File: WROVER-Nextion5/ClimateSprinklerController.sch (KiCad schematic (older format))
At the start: 177 parts, among them J1 7.5 TO 40 V, J10 HVAC, J2 USB_B_Micro, J3 POWER_SEL, J4 NEXTION, J5 SERIAL, J6 SPI, J7 PIR, J8 I2C, J9 IO_EXP, K1 G6E-134P-US DC5, Q1 MMSS8050, Q2 MMSS8050, Q3 TEPT5700, Q4 2N7002, Q5 2N6073B, Q6 2N6073B, Q7 2N6073B, Q8 2N6073B, Q9 2N6073B, SW1 POWER, SW2 RESET, SW3 MODE, U1 ESP32-WROVER, U10 SHTC3, U11 TMP117, U12 MOC3043, U13 MOC3043, U14 MOC3043, U15 MOC3043, U16 MOC3043, U17 DHT22, U2 MCP23017_SO, U3 FT232RL, U4 TPS22917DBV, U5 LMR36520, U6 SGP40-Sensor_Air_Quality, U7 BME680, U8 LD1086DT33TR, U9 BME280

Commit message: Nextion PCBs tweak
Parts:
- R12, R20: Part RC0805FR-07100KL -> RC0805FR-074R7L
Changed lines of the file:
@@
 F 2 "Resistor_SMD:R_0805_2012Metric_Pad1.20x1.40mm_HandSolder" V 9180 12150 50  0001 C CNN
 F 3 "~" H 9250 12150 50  0001 C CNN
-F 4 "RC0805FR-07100KL" H 9250 12150 50  0001 C CNN "Part"
+F 4 "RC0805FR-074R7L" H 9250 12150 50  0001 C CNN "Part"
 	1    9250 12150
 	1    0    0    -1
@@
 F 2 "Resistor_SMD:R_0805_2012Metric_Pad1.20x1.40mm_HandSolder" V 5980 4700 50  0001 C CNN
 F 3 "~" H 6050 4700 50  0001 C CNN
-F 4 "RC0805FR-07100KL" H 6050 4700 50  0001 C CNN "Part"
+F 4 "RC0805FR-074R7L" H 6050 4700 50  0001 C CNN "Part"
 	1    6050 4700
 	-1   0    0    1

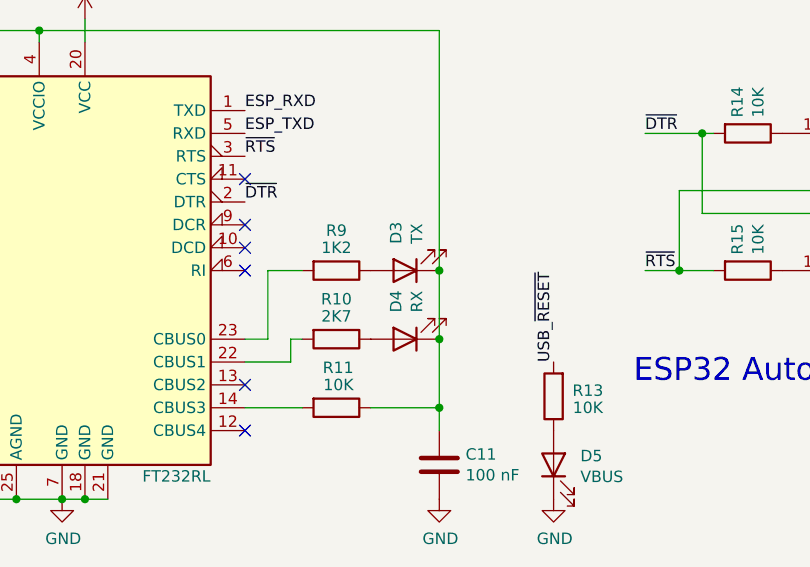
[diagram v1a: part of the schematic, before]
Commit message: TX+RX LEDs were backwards...oops
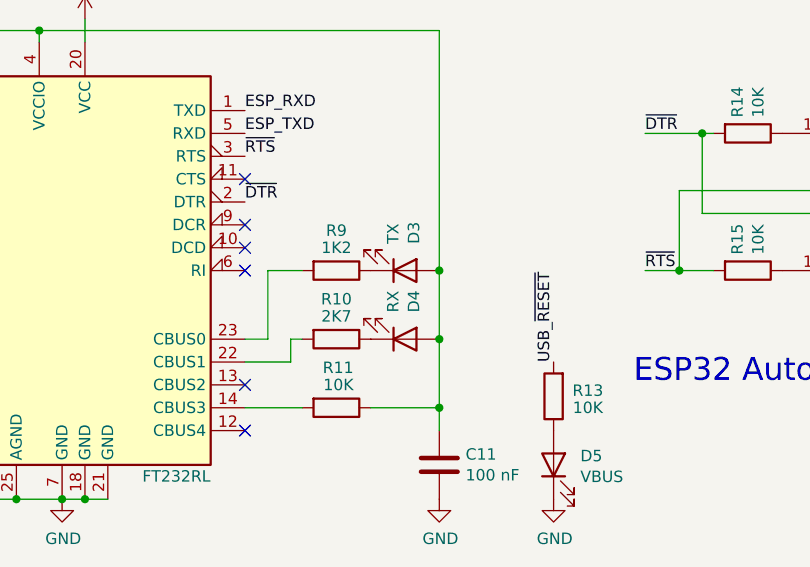
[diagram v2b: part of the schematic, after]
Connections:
- net at C11.1, R11.1, U3.17 (3V3OUT)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: now also D3.2 (A), D4.2 (A); no longer D3.1 (K), D4.1 (K)
- net at R9.1: now also D3.1 (K); no longer D3.2 (A)
- net at R10.1: now also D4.1 (K); no longer D4.2 (A)
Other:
- moved on the sheet: D3, D4
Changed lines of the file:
@@
 F 4 "APTL3216QBC/D" V 5850 12900 50  0001 C CNN "Part"
 	1    5850 12900
-	-1   0    0    1
+	1    0    0    1
 $EndComp
 $Comp
@@
 F 4 "APTL3216SURCK" V 5850 13200 50  0001 C CNN "Part"
 	1    5850 13200
-	-1   0    0    1
+	1    0    0    1
 $EndComp
 Wire Wire Line

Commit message: Doc updates, new images, new enclosures, regenerate gerbers
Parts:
- C1: MPN1 (none) -> C2012X5R1V106K085AC; Part C2012X5R1V106K085AC -> (none)
- C10, C11, C15, C17, C22, C23, C24, C26, C28, C29, C3, C30, C31, C32, C4, C6, C8: MPN1 (none) -> CC0805KRX7R7BB104; Part CC0805KRX7R7BB104 -> (none)
- C12, C2, C5, C9: MPN1 (none) -> C2012X5R1H475K125AB; Part C2012X5R1H475K125AB -> (none)
- C13: MPN1 (none) -> C2012X5R1H224K125AA; Part C2012X5R1H224K125AA -> (none)
- C14, C19, C20: MPN1 (none) -> C0805C105K4RACTU; Part C0805C105K4RACTU -> (none)
- C16, C18, C21: MPN1 (none) -> GRM32ER61C476KE15L; Part GRM32ER61C476KE15L -> (none)
- C25, C27: MPN1 (none) -> EEE-HP0J100R; Part EEE-HP0J100R -> (none)
- C33, C34, C35, C36, C37: MPN1 (none) -> CC0805KRX7R9BB103; Part CC0805KRX7R9BB103 -> (none)
- C7: MPN1 (none) -> UVK1H471MPD; Part UVK1H471MPD -> (none)
- D1: value MBR230S1F-7 -> N/A; MPN1 (none) -> MBR230S1F-7; Part MBR230S1F-7 -> (none)
- D10: MPN1 (none) -> APTL3216CGCK; Part APTL3216CGCK -> (none)
- D11, D5: MPN1 (none) -> APTL3216ZGC; Part APTL3216ZGC -> (none)
- D12, D13, D3: MPN1 (none) -> APTL3216QBC/D; Part APTL3216QBC/D -> (none)
- D14, D15, D4: MPN1 (none) -> APTL3216SURCK; Part APTL3216SURCK -> (none)
- D2: value CD-MBL206SL -> N/A; MPN1 (none) -> CD-MBL206SL; Part CD-MBL206SL -> (none)
- D6, D7: MPN1 (none) -> 597-6901-607F; Part 597-6901-607F -> (none)
- D8: MPN1 (none) -> APTL3216SECK; Part APTL3216SECK -> (none)
- D9: value 1N4148 -> N/A; MPN1 (none) -> 1N4148W; Part 1N4148W -> (none)
- F1: MPN1 (none) -> 2920L030DR; Part 2920L030DR -> (none)
- H1, H2, H3, H4, H5, H6, H7, H8, J3, J4, J5, J6, J7, J8, J9, JP1, JP10, JP11, JP12, JP13, JP14, JP15, JP16, JP17, JP2, JP3, JP4, JP5, JP6, JP7, JP8, JP9: MPN1 (none) -> N/A; Population (none) -> DNF
- J1: MPN1 (none) -> 694106301002; Part 694106301002 -> (none)
- J10: MPN1 (none) -> 1862039; Part 1862039 -> (none)
- J2: value USB_B_Micro -> N/A; MPN1 (none) -> 105017-0001; Part 105017-0001 -> (none)
- K1: MPN1 (none) -> G6E-134P-US DC5; Part G6E-134P-US DC5 -> (none)
- L1: MPN1 (none) -> 7447709150; MPN2 (none) -> MSS1210-153MEB; Part 7447709150 -> (none); PartAlt MSS1210-153MEB -> (none)
- Q1, Q2: MPN1 (none) -> MMSS8050; Part MMSS8050 -> (none)
- Q3: MPN1 (none) -> TEPT5700; Part TEPT5700 -> (none)
- Q4: MPN1 (none) -> 2N7002; Part 2N7002 -> (none)
- Q5, Q6, Q7, Q8, Q9: value 2N6073B -> 2N6073BG; MPN1 (none) -> 2N6073BG; Part 2N6073BG -> (none)
- R1, R11, R14, R15, R2, R22, R25, R26, R3, R5, R50, R6, R7, R8: MPN1 (none) -> RC0805FR-0710KL; Part RC0805FR-0710KL -> (none)
- R10, R33, R34, R9: MPN1 (none) -> RT0805FRE072K7L; Part RT0805FRE072K7L -> (none)
- R12, R20: MPN1 (none) -> RC0805FR-074R7L; Part RC0805FR-074R7L -> (none)
- R13, R30: MPN1 (none) -> RC0805FR-0710KL; Part RT0805FRE079K1L -> (none)
- R16, R19: MPN1 (none) -> RC0805FR-07100KL; Part RC0805FR-07100KL -> (none)
- R17: MPN1 (none) -> RT0805FRE0724K9L; Part RT0805FRE0724K9L -> (none)
- R18, R21: MPN1 (none) -> RT0805FRE073K3L; Part RT0805FRE073K3L -> (none)
- R23: MPN1 (none) -> CRCW08055K00JNTA; Part CRCW08055K00JNTA -> (none)
- R24: MPN1 (none) -> RT0805FRE078K2L; Part RT0805FRE078K2L -> (none)
- R27: MPN1 (none) -> RT0805FRE071K6L; Part RT0805FRE071K6L -> (none)
- R28: MPN1 (none) -> RT0805FRE07120RL; Part RT0805FRE07120RL -> (none)
- R29: value 1K2 -> 560; MPN1 (none) -> RT0805FRE07560RL; Part RT0805FRE071K2L -> (none)
- R31, R32: value 1K2 -> 1K5; MPN1 (none) -> RT0805FRE071K5L; Part RT0805FRE072K7L -> (none)
- R35, R36, R37, R38, R39: MPN1 (none) -> RT0805FRE07270RL; Part RT0805FRE07270RL -> (none)
- R4: MPN1 (none) -> RT0805FRE074K7L; Part RT0805FRE074K7L -> (none)
- R40, R41, R42, R43, R44: MPN1 (none) -> RT0805FRE07180RL; Part RT0805FRE07180RL -> (none)
- R45, R46, R47, R48, R49: MPN1 (none) -> RT0805FRE07820RL; Part RT0805FRE07820RL -> (none)
- R51, R52, R53, R54, R55: MPN1 (none) -> ERJ-P06J390V; Part ERJ-P06J390V -> (none)
- RV1: value B72205S0400K101 -> N/A; MPN1 (none) -> B72205S0400K101; Part B72205S0400K101 -> (none)
- SW1: MPN1 (none) -> 48BFSP1M6QT; Part 48BFSP1M6QT -> (none)
- SW2, SW3: MPN1 (none) -> PTS645VK582LFS; Part PTS645VK582LFS -> (none)
- TH1, TH2: value NXFT15XH103FA2B100 -> 10K; MPN1 (none) -> NXFT15XH103FA2B100; Part NXFT15XH103FA2B100 -> (none)
- U1: MPN1 (none) -> ESP32-WROVER; Part ESP32-WROVER -> (none)
- U10: MPN1 (none) -> SHTC3; Part SHTC3 -> (none)
- U11: MPN1 (none) -> TMP117MAIDRVR; Part TMP117MAIDRVR -> (none)
- U12, U13, U14, U15, U16: MPN1 (none) -> MOC3043SM; Part MOC3043SM -> (none)
- U17: MPN1 (none) -> DHT22; Part DHT22 -> (none)
- U2: MPN1 (none) -> MCP23017-E/SO; Part MCP23017-E/SO -> (none)
- U3: MPN1 (none) -> FT232RL; Part FT232RL -> (none)
- U4: MPN1 (none) -> TPS22917DBV; Part TPS22917DBV -> (none)
- U5: MPN1 (none) -> LMR36520ADDAR; Part LMR36520ADDAR -> (none)
- U6: value SGP40-Sensor_Air_Quality -> SGP40; MPN1 (none) -> SGP40; Part SGP40 -> (none)
- U7: MPN1 (none) -> BME680; Part BME680 -> (none)
- U8: MPN1 (none) -> LD1086DT33TR; Part LD1086DT33TR -> (none)
- U9: MPN1 (none) -> BME280; Part BME280 -> (none)
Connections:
- net +3V3: now also C32.1, U17.1 (VCC)
- net +5V: no longer C32.1, U17.1 (VCC)
